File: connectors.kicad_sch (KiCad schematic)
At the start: 53 parts, among them J10 Conn_01x10, J6 Conn_01x03, J7 Conn_01x05, J8 Conn_01x07, J9 Conn_01x06, Q5 AO3400A

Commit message: da
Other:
- company: (none) -> TampanTech
- title: (none) -> Connector
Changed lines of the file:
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@@
 	(generator_version "8.0")
 	(paper "A4")
+	(title_block
+		(title "Connector")
+		(date "2024-09-08")
+		(rev "1")
+		(company "TampanTech")
+		(comment 1 "Drone Flight Management Unit")
+	)
 	(junction
 		(at 177.8 49.53)

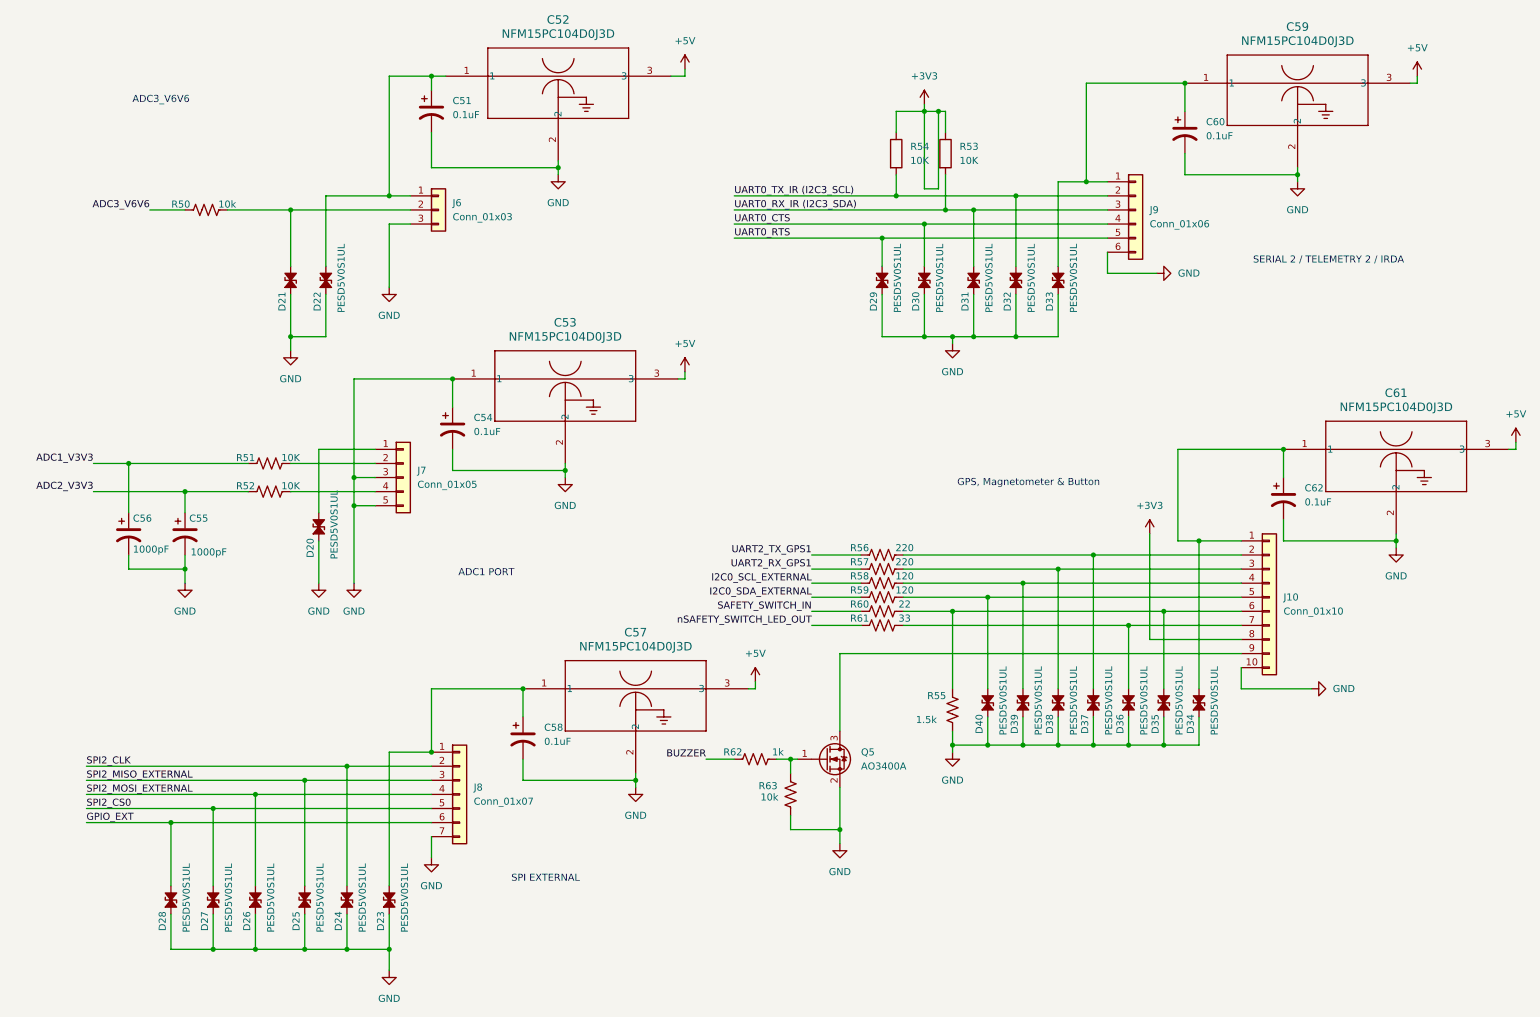
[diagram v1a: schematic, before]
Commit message: change label to global
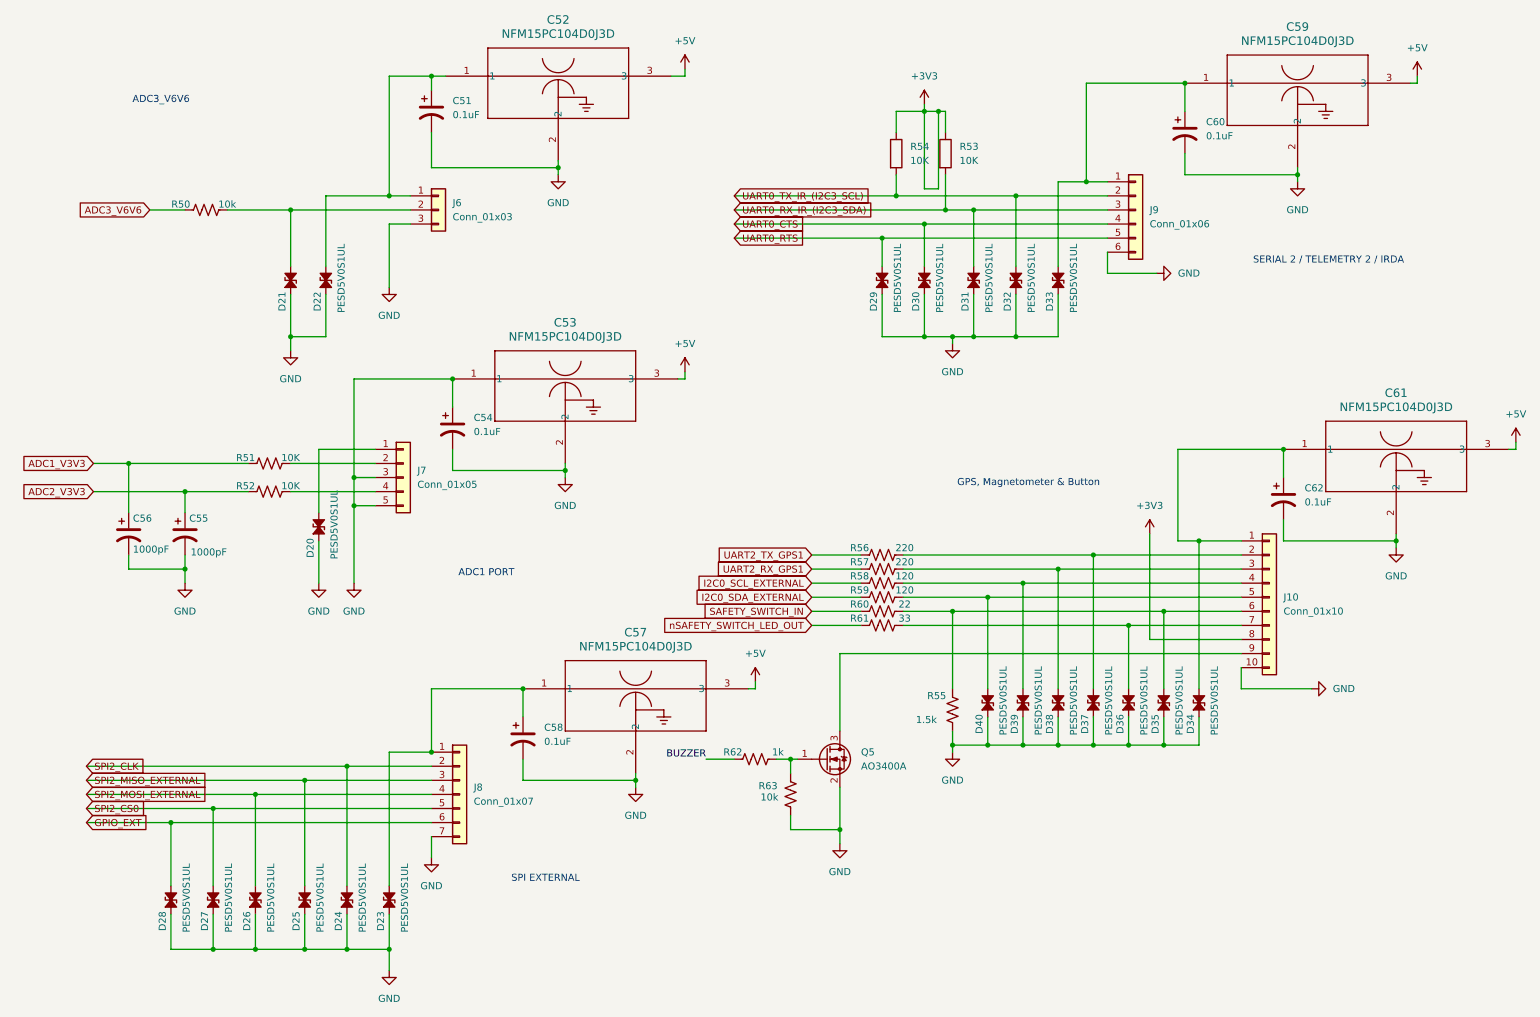
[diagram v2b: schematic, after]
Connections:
- net UART0_RX_IR (I2C3_SDA) renamed UART0_RX_IR_(I2C3_SDA)
- net UART0_TX_IR (I2C3_SCL) renamed UART0_TX_IR_(I2C3_SCL)

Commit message: change label to global
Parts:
- C52, C53, C57, C59, C61: footprint 3PAD_NFM15PC_0402_MUR -> (none)
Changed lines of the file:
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@@
 			)
 		)
-		(property "Footprint" "3PAD_NFM15PC_0402_MUR"
+		(property "Footprint" ""
 			(at 101.6 135.89 0)
 			(effects
@@
 			)
 		)
-		(property "Footprint" "3PAD_NFM15PC_0402_MUR"
+		(property "Footprint" ""
 			(at 238.76 92.71 0)
 			(effects
@@
 			)
 		)
-		(property "Footprint" "3PAD_NFM15PC_0402_MUR"
+		(property "Footprint" ""
 			(at 220.98 26.67 0)
 			(effects
@@
 			)
 		)
-		(property "Footprint" "3PAD_NFM15PC_0402_MUR"
+		(property "Footprint" ""
 			(at 87.63 25.4 0)
 			(effects
@@
 			)
 		)
-		(property "Footprint" "3PAD_NFM15PC_0402_MUR"
+		(property "Footprint" ""
 			(at 88.9 80.01 0)
 			(effects
